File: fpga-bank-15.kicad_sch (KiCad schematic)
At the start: 1 part

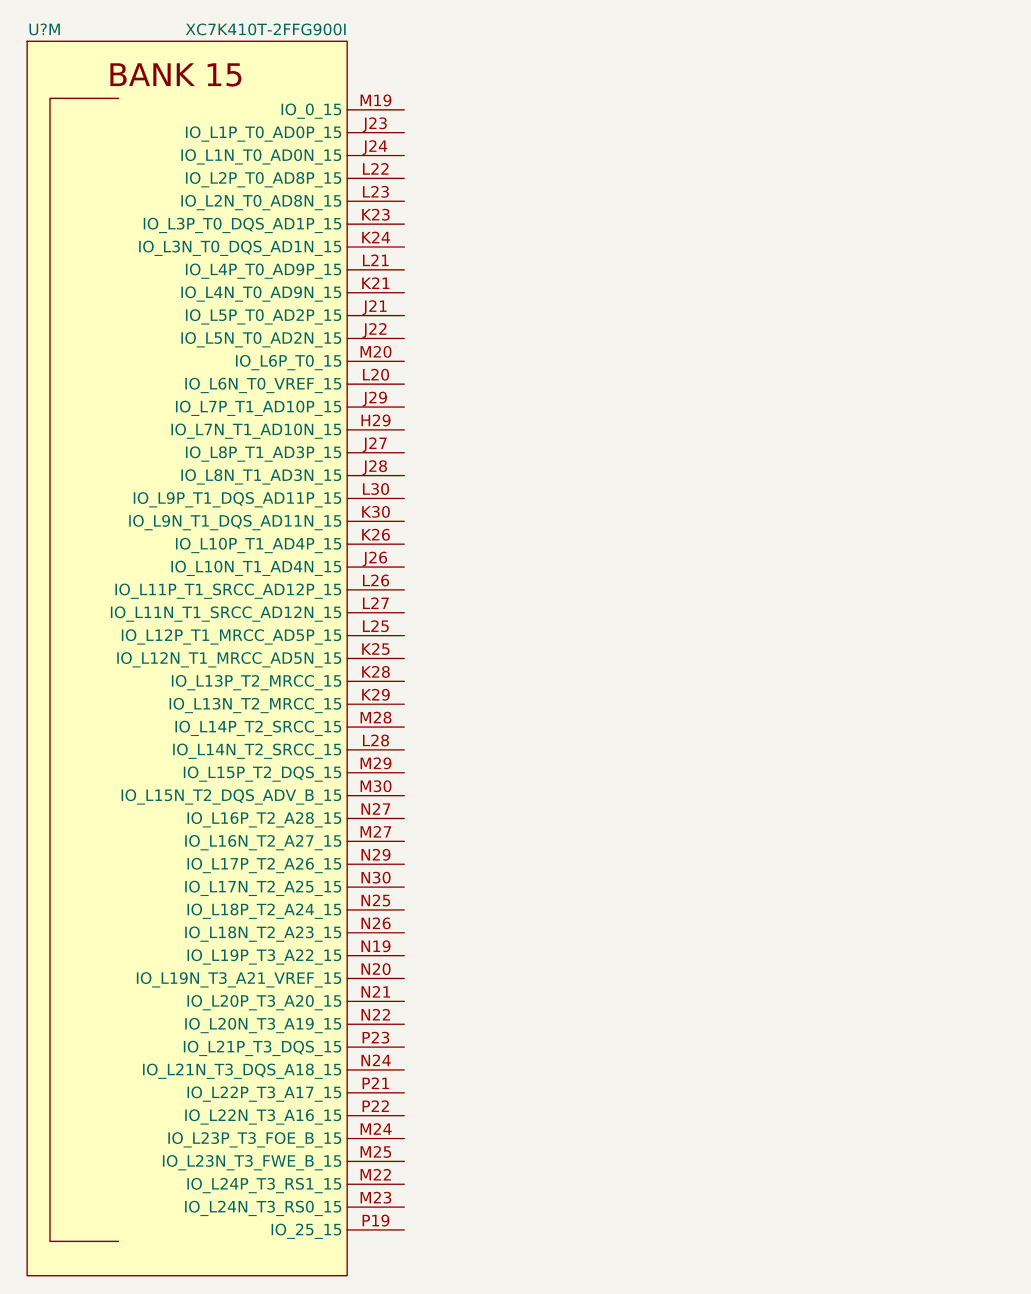
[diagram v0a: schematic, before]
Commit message: Add 40pin and 34pin gpio headers, connect them to FPGA
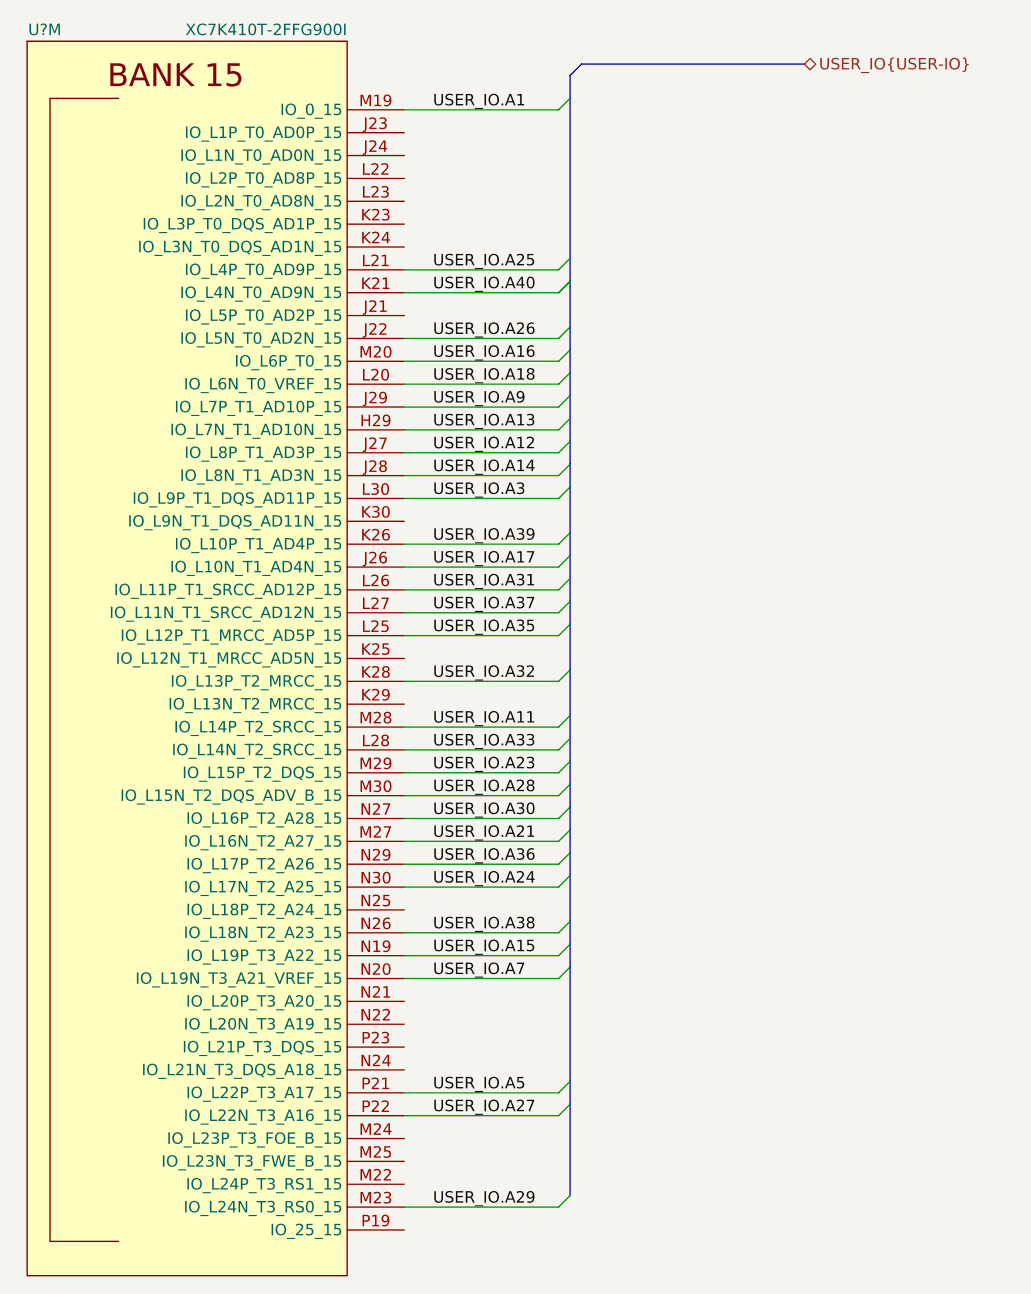
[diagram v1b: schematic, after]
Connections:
- net USER_IO.A13: now reaches U?.H29 (IO_L7N_T1_AD10N_15)
- net USER_IO.A26: now reaches U?.J22 (IO_L5N_T0_AD2N_15)
- net USER_IO.A17: now reaches U?.J26 (IO_L10N_T1_AD4N_15)
- net USER_IO.A12: now reaches U?.J27 (IO_L8P_T1_AD3P_15)
- net USER_IO.A14: now reaches U?.J28 (IO_L8N_T1_AD3N_15)
- net USER_IO.A9: now reaches U?.J29 (IO_L7P_T1_AD10P_15)
- net USER_IO.A40: now reaches U?.K21 (IO_L4N_T0_AD9N_15)
- net USER_IO.A39: now reaches U?.K26 (IO_L10P_T1_AD4P_15)
- net USER_IO.A32: now reaches U?.K28 (IO_L13P_T2_MRCC_15)
- net USER_IO.A18: now reaches U?.L20 (IO_L6N_T0_VREF_15)
- net USER_IO.A25: now reaches U?.L21 (IO_L4P_T0_AD9P_15)
- net USER_IO.A35: now reaches U?.L25 (IO_L12P_T1_MRCC_AD5P_15)
- net USER_IO.A31: now reaches U?.L26 (IO_L11P_T1_SRCC_AD12P_15)
- net USER_IO.A37: now reaches U?.L27 (IO_L11N_T1_SRCC_AD12N_15)
- net USER_IO.A33: now reaches U?.L28 (IO_L14N_T2_SRCC_15)
- net USER_IO.A3: now reaches U?.L30 (IO_L9P_T1_DQS_AD11P_15)
- net USER_IO.A1: now reaches U?.M19 (IO_0_15)
- net USER_IO.A16: now reaches U?.M20 (IO_L6P_T0_15)
- net USER_IO.A29: now reaches U?.M23 (IO_L24N_T3_RS0_15)
- net USER_IO.A21: now reaches U?.M27 (IO_L16N_T2_A27_15)
- net USER_IO.A11: now reaches U?.M28 (IO_L14P_T2_SRCC_15)
- net USER_IO.A23: now reaches U?.M29 (IO_L15P_T2_DQS_15)
- net USER_IO.A28: now reaches U?.M30 (IO_L15N_T2_DQS_ADV_B_15)
- net USER_IO.A15: now reaches U?.N19 (IO_L19P_T3_A22_15)
- net USER_IO.A7: now reaches U?.N20 (IO_L19N_T3_A21_VREF_15)
- net USER_IO.A38: now reaches U?.N26 (IO_L18N_T2_A23_15)
- net USER_IO.A30: now reaches U?.N27 (IO_L16P_T2_A28_15)
- net USER_IO.A36: now reaches U?.N29 (IO_L17P_T2_A26_15)
- net USER_IO.A24: now reaches U?.N30 (IO_L17N_T2_A25_15)
- net USER_IO.A5: now reaches U?.P21 (IO_L22P_T3_A17_15)
- net USER_IO.A27: now reaches U?.P22 (IO_L22N_T3_A16_15)

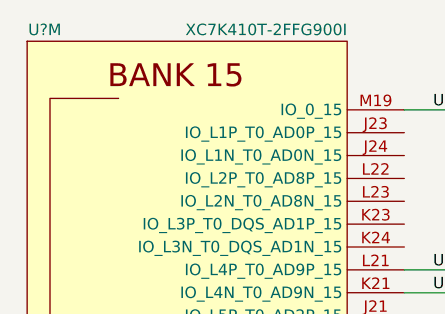
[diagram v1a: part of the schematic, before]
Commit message: Fix FPGA symbol
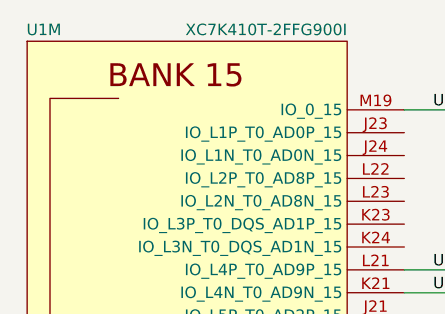
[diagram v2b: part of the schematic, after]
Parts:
- gave numbers to parts that had none: 1
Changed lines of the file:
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@@
     (effects (font (size 1.27 1.27)) (justify left))
   )
-  (symbol (lib_name "XC7K410T-2FFG900I_1") (lib_id "antmicroMicrocontrollers:XC7K410T-2FFG900I") (at 119.38 144.78 0) (unit 13)
+  (symbol (lib_id "antmicroMicrocontrollers:XC7K410T-2FFG900I") (at 119.38 144.78 0) (unit 13)
     (in_bom yes) (on_board yes)
-    (property "Reference" "U?" (id 0) (at 105.41 74.93 0)
+    (property "Reference" "U1" (id 0) (at 105.41 74.93 0)
       (effects (font (size 1.27 1.27)) (justify right))
     )

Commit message: Loclib
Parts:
- U1: footprint antmicro-footprints:xc7k410t-2ffg900I -> K410T-devboard-footprints:xc7k410t-2ffg900I; symbol antmicroMicrocontrollers:XC7K410T-2FFG900I -> K410T-devboard:XC7K410T-2FFG900I

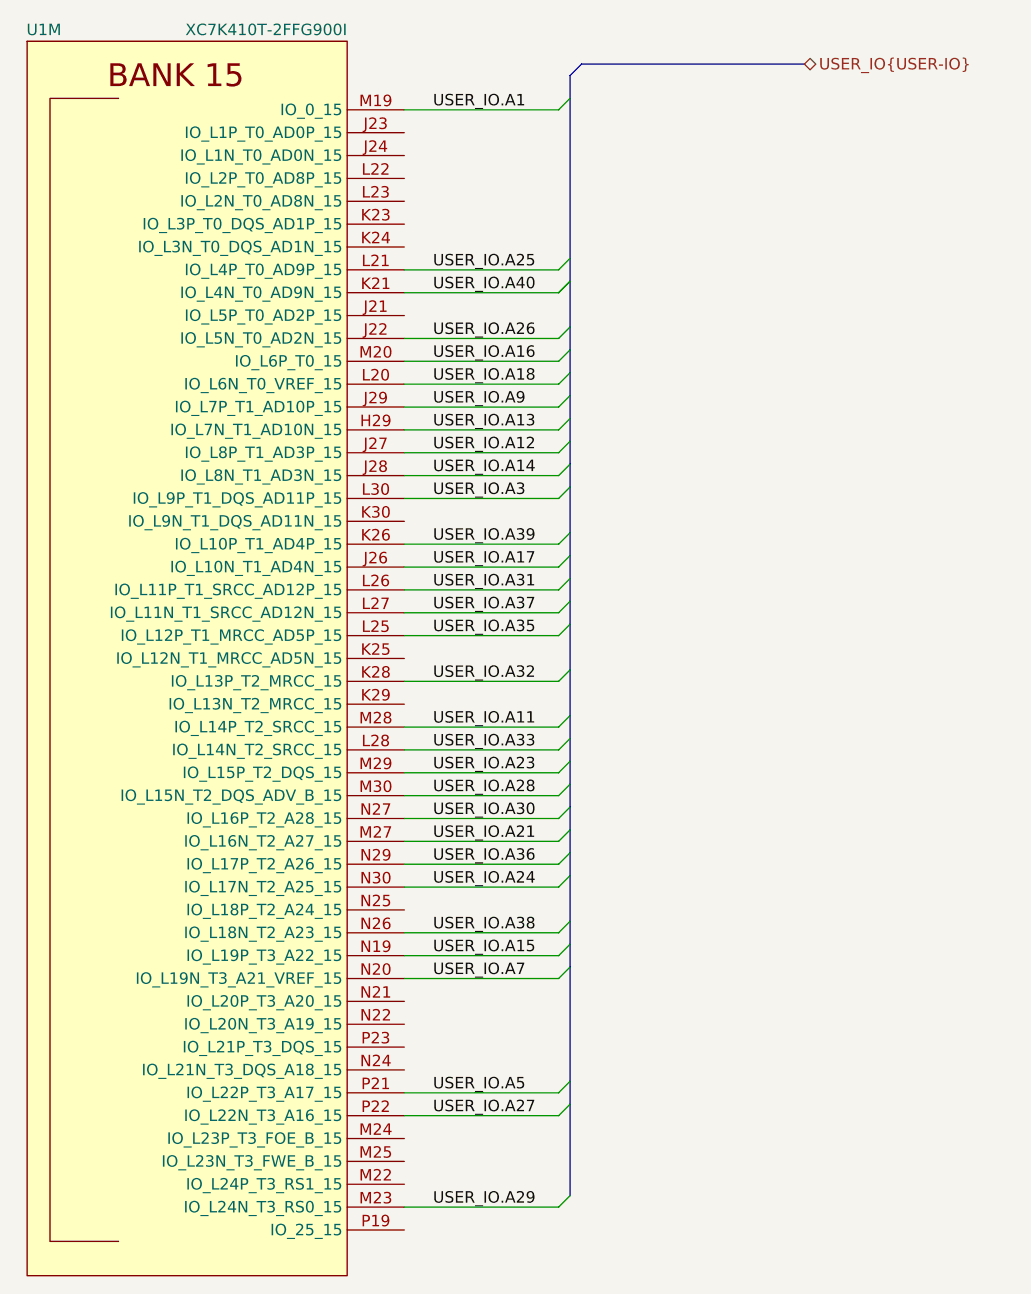
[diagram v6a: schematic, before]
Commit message: Corrected schematic according to review
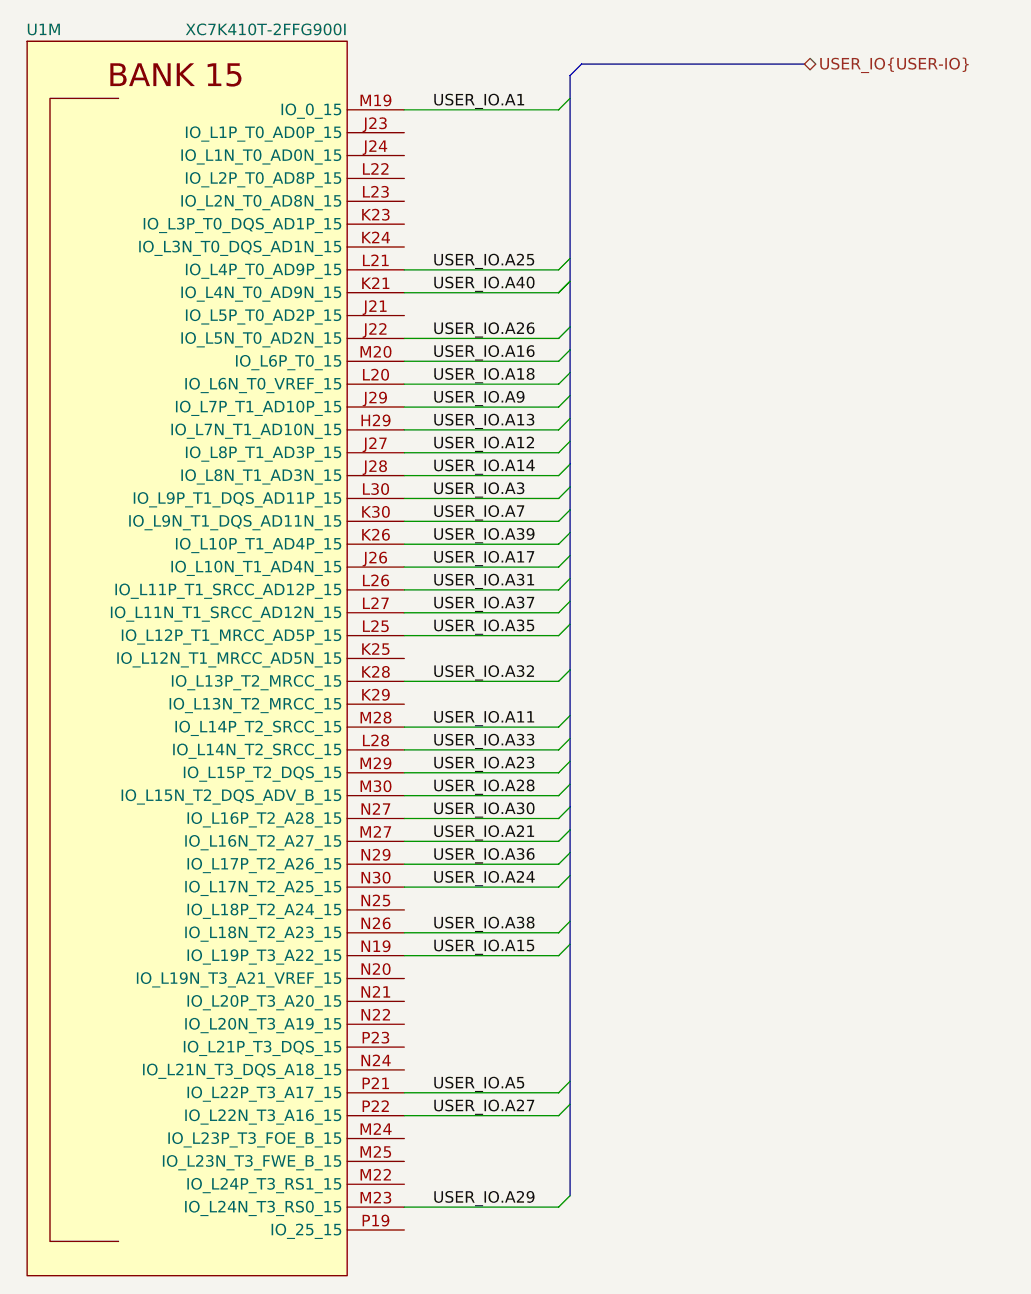
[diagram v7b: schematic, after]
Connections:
- net USER_IO.A7: now also U1.K30 (IO_L9N_T1_DQS_AD11N_15); no longer U1.N20 (IO_L19N_T3_A21_VREF_15)
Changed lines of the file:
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@@
     (stroke (width 0) (type default) (color 0 0 0 0))
   )
-  (bus_entry (at 161.925 179.07) (size -1.27 1.27)
+  (bus_entry (at 161.925 128.27) (size -1.27 1.27)
     (stroke (width 0) (type default) (color 0 0 0 0))
   )
@@
     (stroke (width 0) (type default) (color 0 0 0 0))
   )
-  (bus (pts (xy 161.925 176.53) (xy 161.925 179.07))
-    (stroke (width 0) (type default) (color 0 0 0 0))
-  )
   (bus (pts (xy 163.195 78.74) (xy 161.925 80.01))
     (stroke (width 0) (type default) (color 0 0 0 0))
@@
     (stroke (width 0) (type default) (color 0 0 0 0))
   )
-  (wire (pts (xy 160.655 180.34) (xy 143.51 180.34))
+  (wire (pts (xy 160.655 129.54) (xy 143.51 129.54))
+    (stroke (width 0) (type default) (color 0 0 0 0))
+  )
+  (bus (pts (xy 161.925 128.27) (xy 161.925 130.81))
     (stroke (width 0) (type default) (color 0 0 0 0))
   )
@@
     (stroke (width 0) (type default) (color 0 0 0 0))
   )
-  (bus (pts (xy 161.925 125.73) (xy 161.925 130.81))
+  (bus (pts (xy 161.925 125.73) (xy 161.925 128.27))
     (stroke (width 0) (type default) (color 0 0 0 0))
   )
@@
     (stroke (width 0) (type default) (color 0 0 0 0))
   )
-  (bus (pts (xy 161.925 179.07) (xy 161.925 191.77))
+  (bus (pts (xy 161.925 176.53) (xy 161.925 191.77))
     (stroke (width 0) (type default) (color 0 0 0 0))
   )
@@
     (effects (font (size 1.27 1.27)) (justify left bottom))
   )
-  (label "USER_IO.A7" (at 146.685 180.34 0)
+  (label "USER_IO.A7" (at 146.685 129.54 0)
     (effects (font (size 1.27 1.27)) (justify left bottom))
   )
